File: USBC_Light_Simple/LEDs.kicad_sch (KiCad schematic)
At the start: 10 parts, among them U1 XHP50B-00-0000-0D0BJ440E, U2 AL8861MP-13, U3 XHP50B-00-0000-0D0BJ440E, U4 XHP50B-00-0000-0D0BJ440E, U6 AL8861MP-13, U7 XHP50B-00-0000-0D0BJ440E, U8 XHP50B-00-0000-0D0BJ440E, U9 XHP50B-00-0000-0D0BJ440E

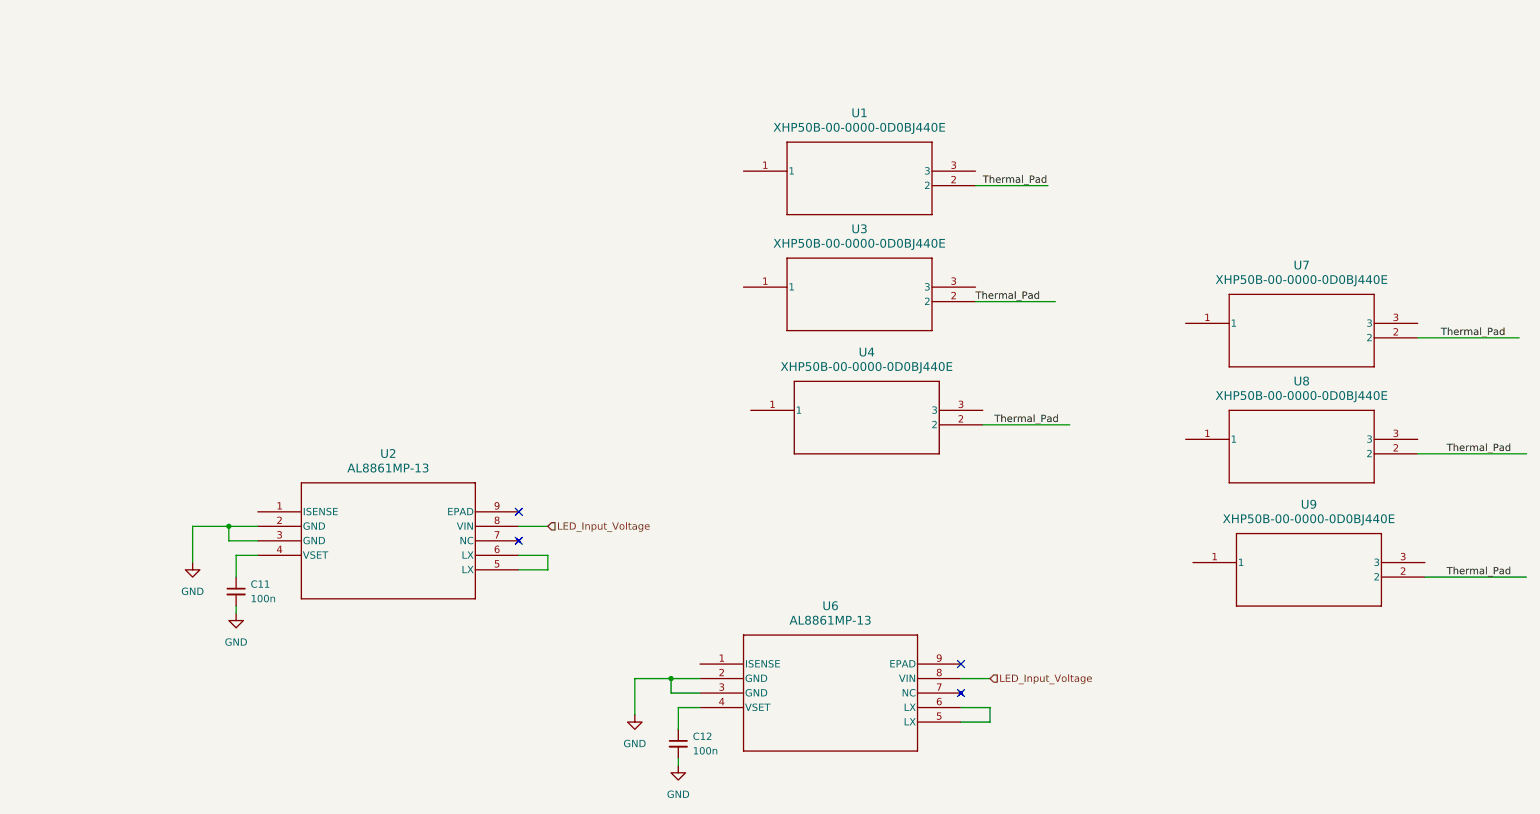
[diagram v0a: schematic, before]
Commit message: Fleshed out most of schematic. Now need to add component vals.
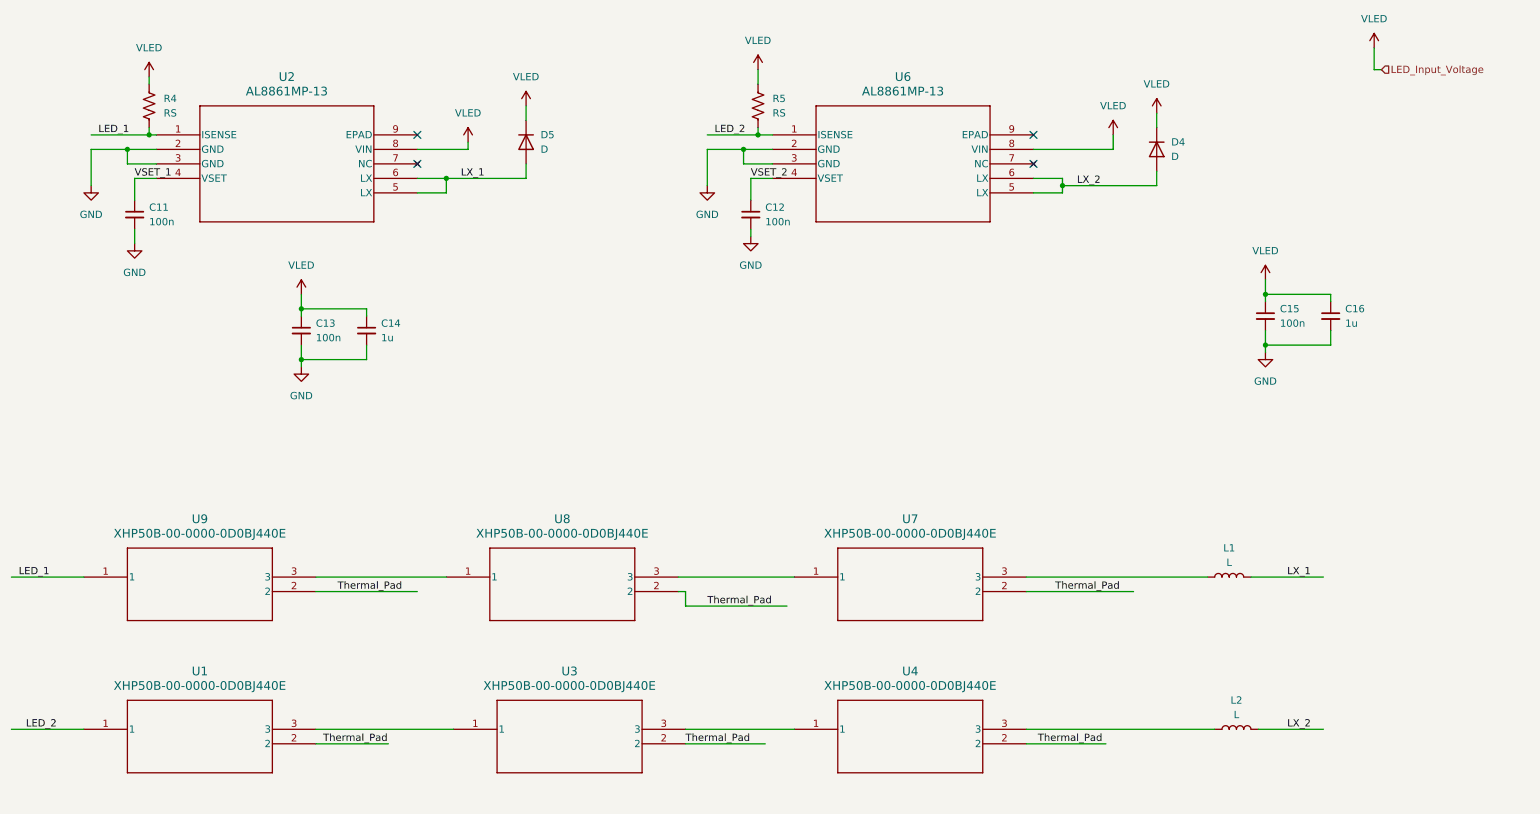
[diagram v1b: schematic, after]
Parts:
- added C13, C15: 100n, symbol Device:C_Small
- added C14, C16: 1u, symbol Device:C_Small
- added D4, D5: D, symbol Device:D
- added L1, L2: L, symbol Device:L
- added R4, R5: RS, symbol Device:R_US
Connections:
- net GND: now also C13.2, C14.2, C15.2, C16.2
- net at U3.1: now also U1.3
- net at U3.3: now also U4.1
- net LED_1: now reaches U9.1
- net LED_1: now also U2.1 (ISENSE), R4.2
- net at U9.3: now also U8.1
- net VSET_1: now reaches C11.1, U2.4 (VSET)
- net at U7.1: now also U8.3
- net at U7.3: now also L1.1
- net VSET_2: now reaches C12.1, U6.4 (VSET)
- net LED_2: now reaches U6.1 (ISENSE)
- net LED_2: now also U1.1, R5.2
- net LX_2: now reaches U6.5 (LX), U6.6 (LX)
- net LX_2: now also D4.2 (A), L2.2
- net LX_1: now reaches U2.5 (LX), U2.6 (LX)
- net LX_1: now also D5.2 (A), L1.2
- net at U4.3: now also L2.1
- net LED_Input_Voltage renamed VLED
- net VLED: now also C13.1, C14.1, C15.1, C16.1, D4.1 (K), D5.1 (K), R4.1, R5.1
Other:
- moved on the sheet: C11, C12, U1, U2, U3, U4, U6, U7, U8, U9

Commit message: Preliminary component placement on board.
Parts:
- C11, C12, C13, C14, C15, C16: footprint (none) -> Capacitor_SMD:C_0603_1608Metric_Pad1.08x0.95mm_HandSolder
- D4, D5: footprint (none) -> Diode_SMD:D_0603_1608Metric
- R4, R5: footprint (none) -> Resistor_SMD:R_0603_1608Metric_Pad0.98x0.95mm_HandSolder
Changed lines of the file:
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@@
 			)
 		)
-		(property "Footprint" ""
+		(property "Footprint" "Capacitor_SMD:C_0603_1608Metric_Pad1.08x0.95mm_HandSolder"
 			(at 77.47 74.93 0)
 			(effects
@@
 			)
 		)
-		(property "Footprint" ""
+		(property "Footprint" "Capacitor_SMD:C_0603_1608Metric_Pad1.08x0.95mm_HandSolder"
 			(at 234.95 72.39 0)
 			(effects
@@
 			)
 		)
-		(property "Footprint" ""
+		(property "Footprint" "Capacitor_SMD:C_0603_1608Metric_Pad1.08x0.95mm_HandSolder"
 			(at 36.83 54.61 0)
 			(effects
@@
 			)
 		)
-		(property "Footprint" ""
+		(property "Footprint" "Capacitor_SMD:C_0603_1608Metric_Pad1.08x0.95mm_HandSolder"
 			(at 246.38 72.39 0)
 			(effects
@@
 			)
 		)
-		(property "Footprint" ""
+		(property "Footprint" "Capacitor_SMD:C_0603_1608Metric_Pad1.08x0.95mm_HandSolder"
 			(at 144.78 54.61 0)
 			(effects
@@
 			)
 		)
-		(property "Footprint" ""
+		(property "Footprint" "Capacitor_SMD:C_0603_1608Metric_Pad1.08x0.95mm_HandSolder"
 			(at 66.04 74.93 0)
 			(effects
@@
 			)
 		)
-		(property "Footprint" ""
+		(property "Footprint" "Diode_SMD:D_0603_1608Metric"
 			(at 215.9 43.18 0)
 			(effects
@@
 			)
 		)
-		(property "Footprint" ""
+		(property "Footprint" "Diode_SMD:D_0603_1608Metric"
 			(at 105.41 41.91 0)
 			(effects
@@
 			)
 		)
-		(property "Footprint" ""
+		(property "Footprint" "Resistor_SMD:R_0603_1608Metric_Pad0.98x0.95mm_HandSolder"
 			(at 40.386 35.814 90)
 			(effects
@@
 			)
 		)
-		(property "Footprint" ""
+		(property "Footprint" "Resistor_SMD:R_0603_1608Metric_Pad0.98x0.95mm_HandSolder"
 			(at 147.066 35.814 90)
 			(effects
